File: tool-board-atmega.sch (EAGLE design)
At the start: 86 parts, among them IC3 ATMEGA2560-16AU, IC4 ATMEGA8U2-MU, Q1 16MHz, X1 22-23-2041, X2 MICROUSB_VERTICAL, X3 22-23-2041, X4 22-23-2041, Y2 16MHz

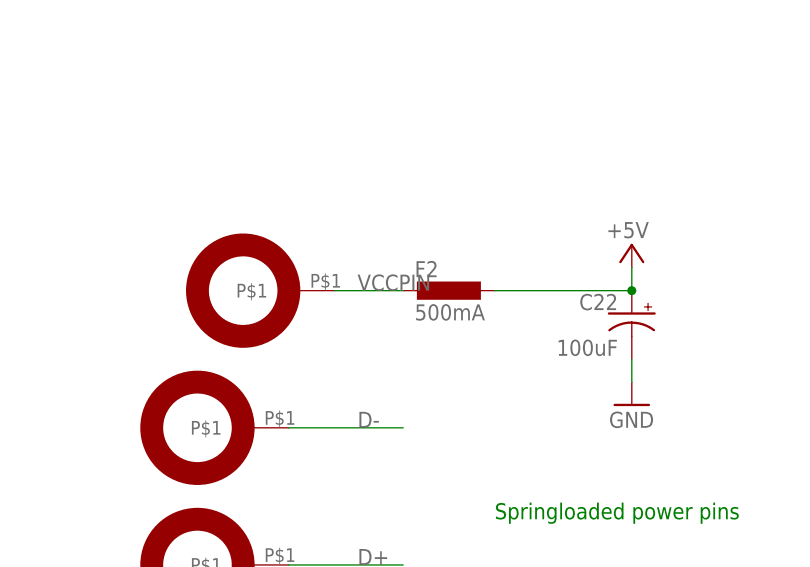
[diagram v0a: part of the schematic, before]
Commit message: significant routing done, need to beef up stepper related lines, add 24V stepper
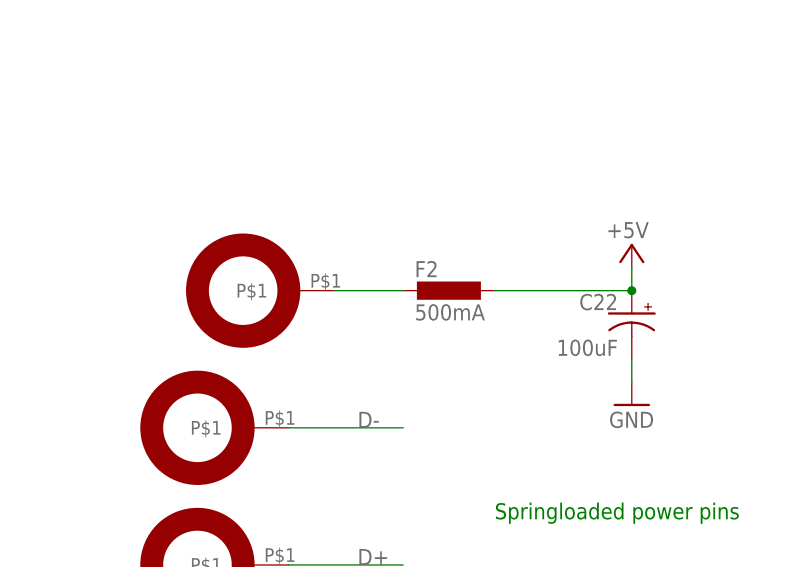
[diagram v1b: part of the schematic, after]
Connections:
- new net N$38: F2.2, U$9.P$1
- net VCCPIN: no longer F2.2, U$9.P$1
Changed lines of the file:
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@@
 <pinref part="X2" gate="G$1" pin="1"/>
-</segment>
-<segment>
-<pinref part="U$9" gate="G$1" pin="P$1"/>
-<wire x1="398.78" y1="-25.4" x2="406.4" y2="-25.4" width="0.1524" layer="91"/>
-<label x="401.32" y="-25.4" size="1.778" layer="95"/>
-<pinref part="F2" gate="G$1" pin="2"/>
 </segment>
 </net>
@@
 </segment>
 </net>
+<net name="N$38" class="0">
+<segment>
+<pinref part="U$9" gate="G$1" pin="P$1"/>
+<pinref part="F2" gate="G$1" pin="2"/>
+<wire x1="398.78" y1="-25.4" x2="406.4" y2="-25.4" width="0.1524" layer="91"/>
+</segment>
+</net>

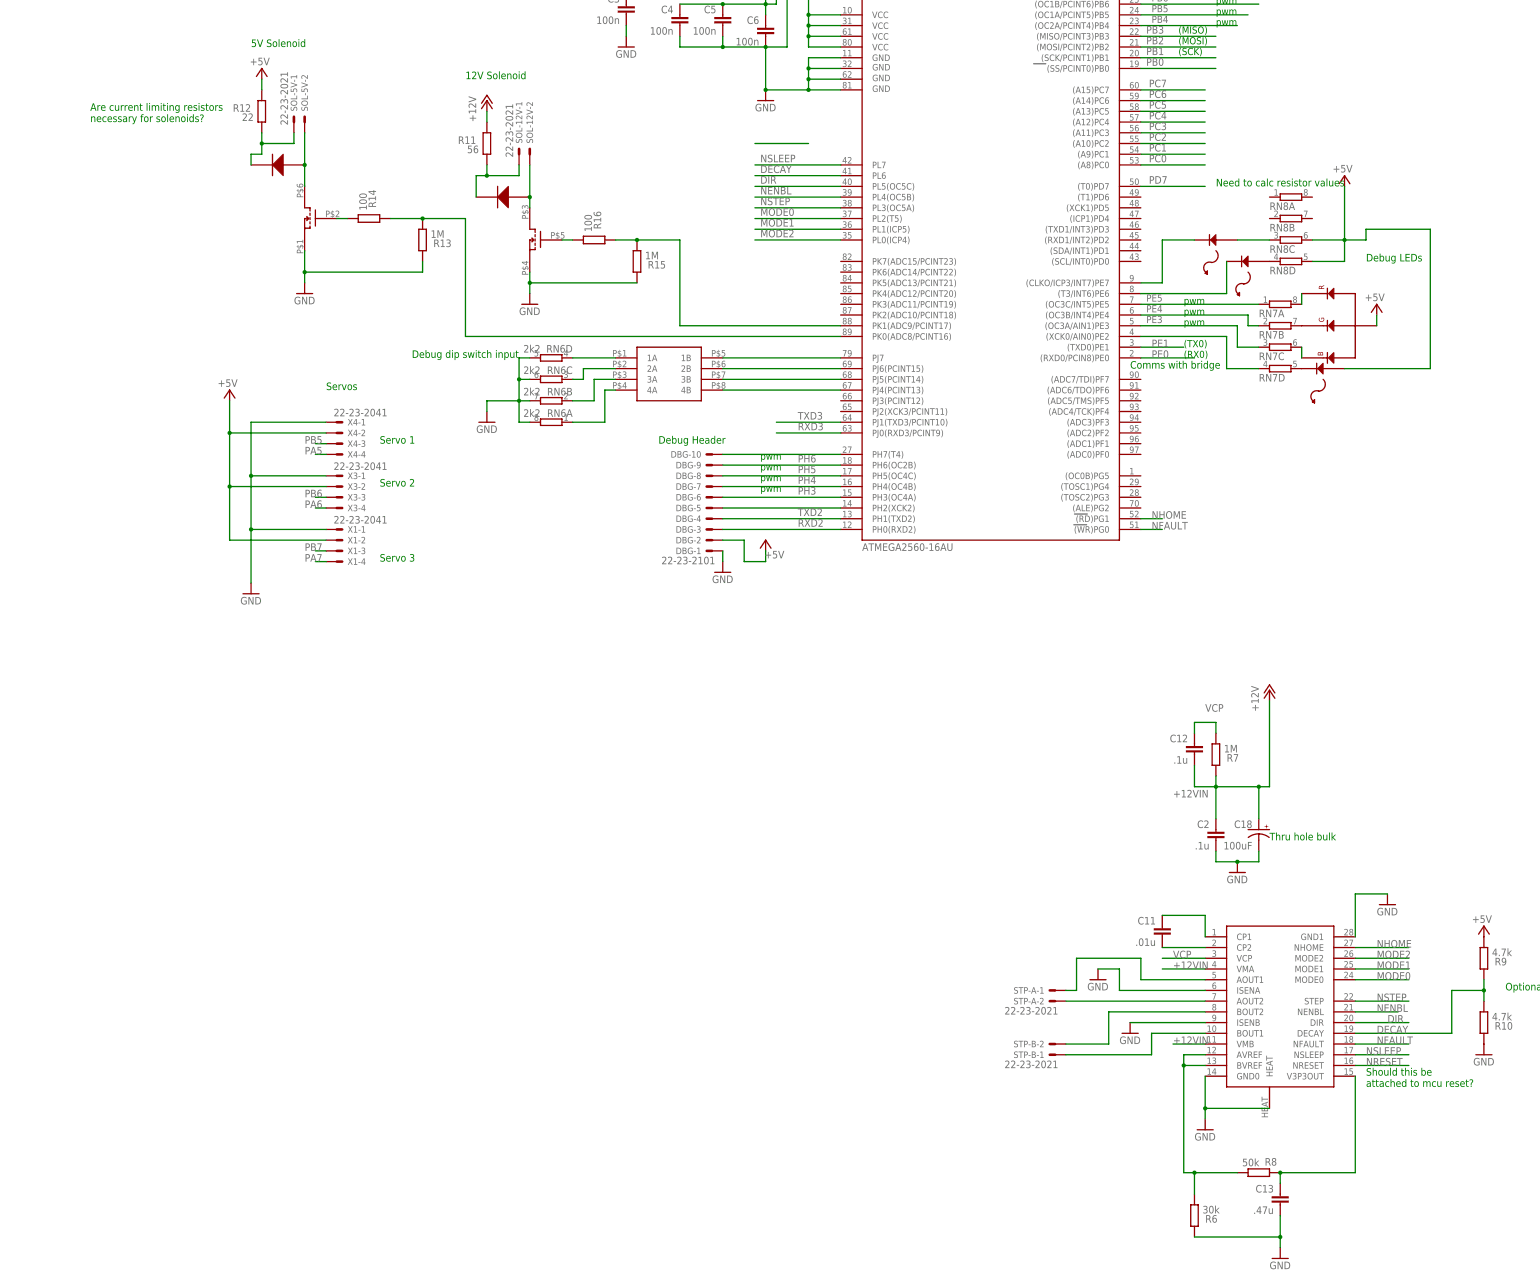
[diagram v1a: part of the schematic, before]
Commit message: Beefed up 12V stepper lines, still need to work on 24V stepper lines.  Need to switch connectors for higher current ones
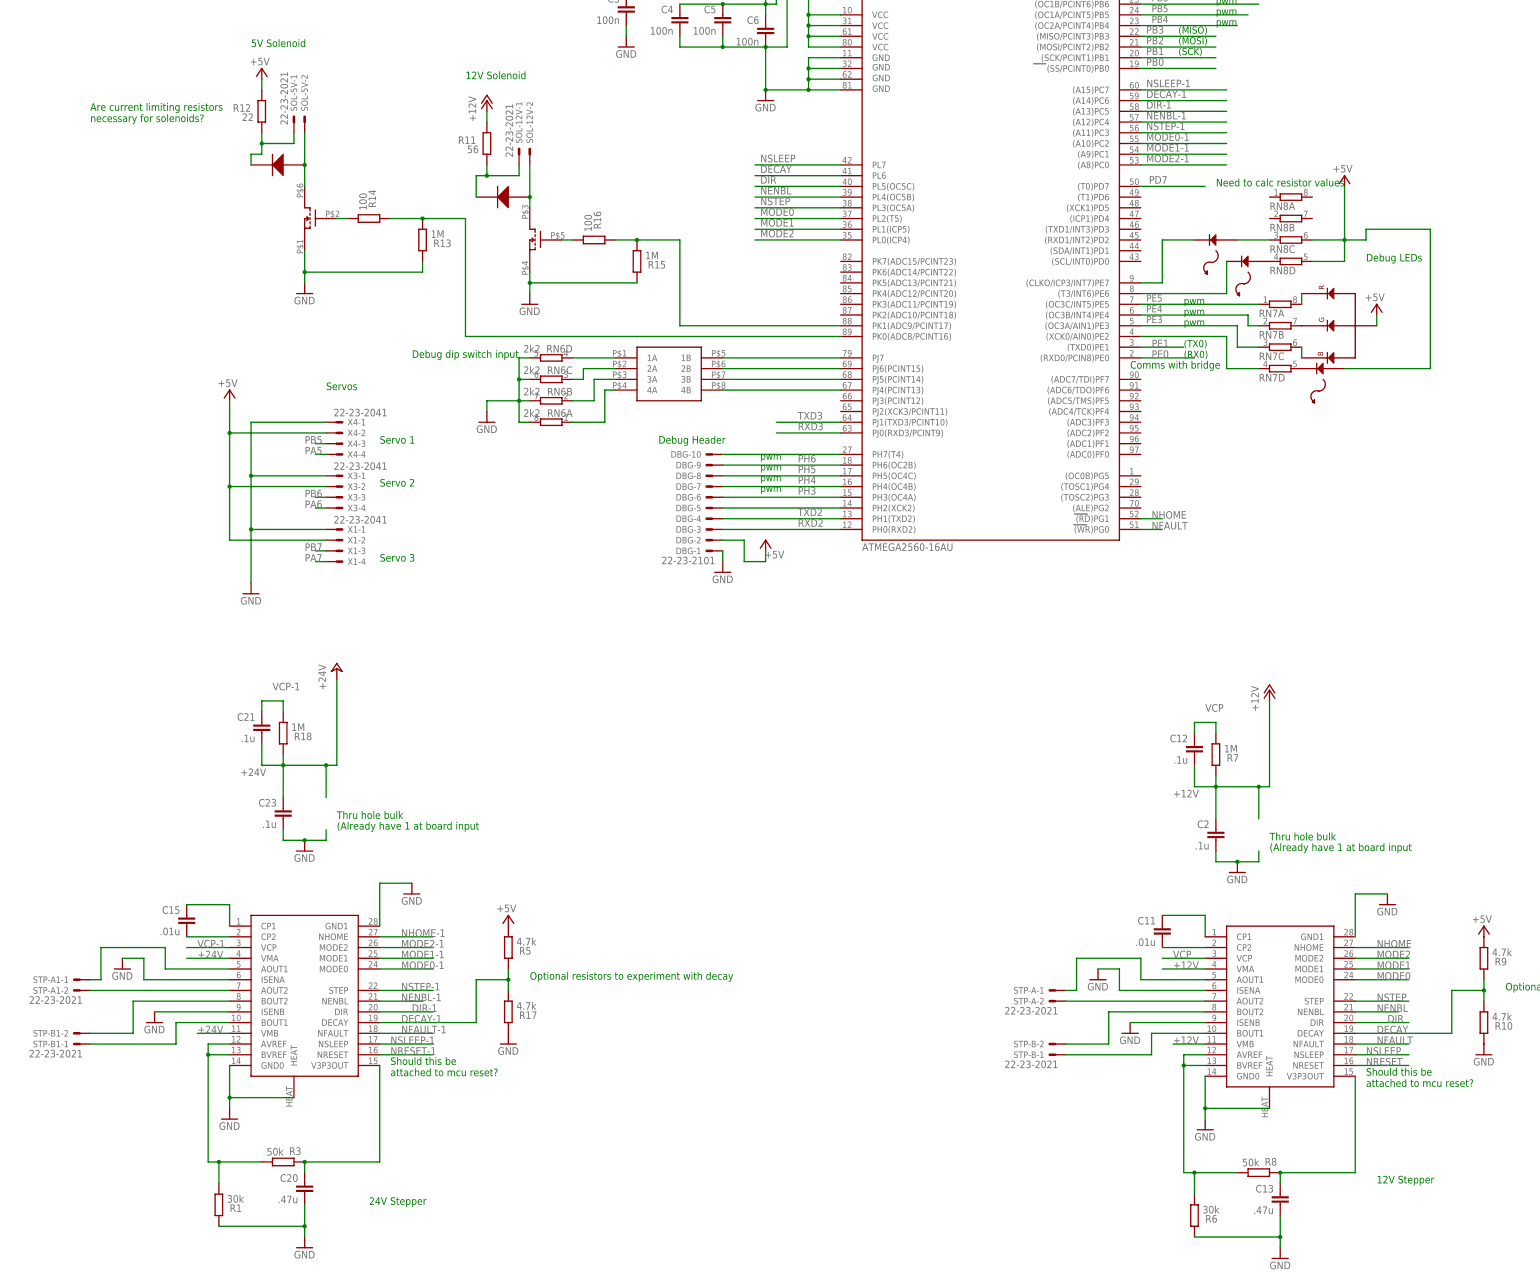
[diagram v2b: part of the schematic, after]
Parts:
- removed C18: 100uF, rcl:CPOL-USE3.5-8
- added C15: .01u, SmartPrj:C-EU0603-RND
- added C20: .47u, SmartPrj:C-EU0603-RND
- added C21, C23: .1u, SmartPrj:C-EU0603-RND
- added R1: 30k, SmartPrj:R-EU_R0603
- added R17, R5: 4.7k, SmartPrj:R-EU_R0603
- added R18: 1M, SmartPrj:R-EU_R0603
- added R3: 50k, SmartPrj:R-EU_R0603
- added STP-A1, STP-B1: 22-23-2021, con-molex:22-23-2021
- added U$7: DRV8825, ClinicalRobotics:DRV8825
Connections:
- removed net +12VIN: C12.2, C18.+, C2.1, R7.2, U$1.VMA, U$1.VMB
- removed net PC0: IC3.(A8)PC0
- removed net PC1: IC3.(A9)PC1
- removed net PC2: IC3.(A10)PC2
- removed net PC3: IC3.(A11)PC3
- removed net PC4: IC3.(A12)PC4
- removed net PC5: IC3.(A13)PC5
- removed net PC6: IC3.(A14)PC6
- removed net PC7: IC3.(A15)PC7
- new net DECAY-1: IC3.(A14)PC6, R17.1, R5.2, U$7.DECAY
- new net DIR-1: IC3.(A13)PC5, U$7.DIR
- new net MODE0-1: IC3.(A10)PC2, U$7.MODE0
- new net MODE1-1: IC3.(A9)PC1, U$7.MODE1
- new net MODE2-1: IC3.(A8)PC0, U$7.MODE2
- new net N$39: C15.1, U$7.CP1
- new net N$40: C15.2, U$7.CP2
- new net N$41: C20.1, R3.2, U$7.V3P3OUT
- new net N$42: R1.1, R3.1, U$7.AVREF, U$7.BVREF
- new net N$43: STP-A1-1.S, U$7.AOUT1
- new net N$44: STP-A1-2.S, U$7.AOUT2
- new net N$45: STP-B1-2.S, U$7.BOUT2
- new net N$46: STP-B1-1.S, U$7.BOUT1
- new net NENBL-1: IC3.(A12)PC4, U$7.NENBL
- new net NFAULT-1: U$7.NFAULT
- new net NHOME-1: U$7.NHOME
- new net NRESET-1: U$7.NRESET
- new net NSLEEP-1: IC3.(A15)PC7, U$7.NSLEEP
- new net NSTEP-1: IC3.(A11)PC3, U$7.STEP
- new net VCP-1: C21.1, R18.1, U$7.VCP
- net +12V: now also C12.2, C2.1, R7.2, U$1.VMA, U$1.VMB
- net +24V: now also C21.2, C23.1, R18.2, U$7.VMA, U$7.VMB
- net +5V: now also R5.1
- net GND: now also C20.2, C23.2, R1.2, R17.2, U$7.GND0, U$7.GND1, U$7.HEAT, U$7.ISENA, U$7.ISENB; no longer C18.-
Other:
- note added: "(Already have 1 at board input"
- note added: "12V Stepper"
- note added: "24V Stepper"

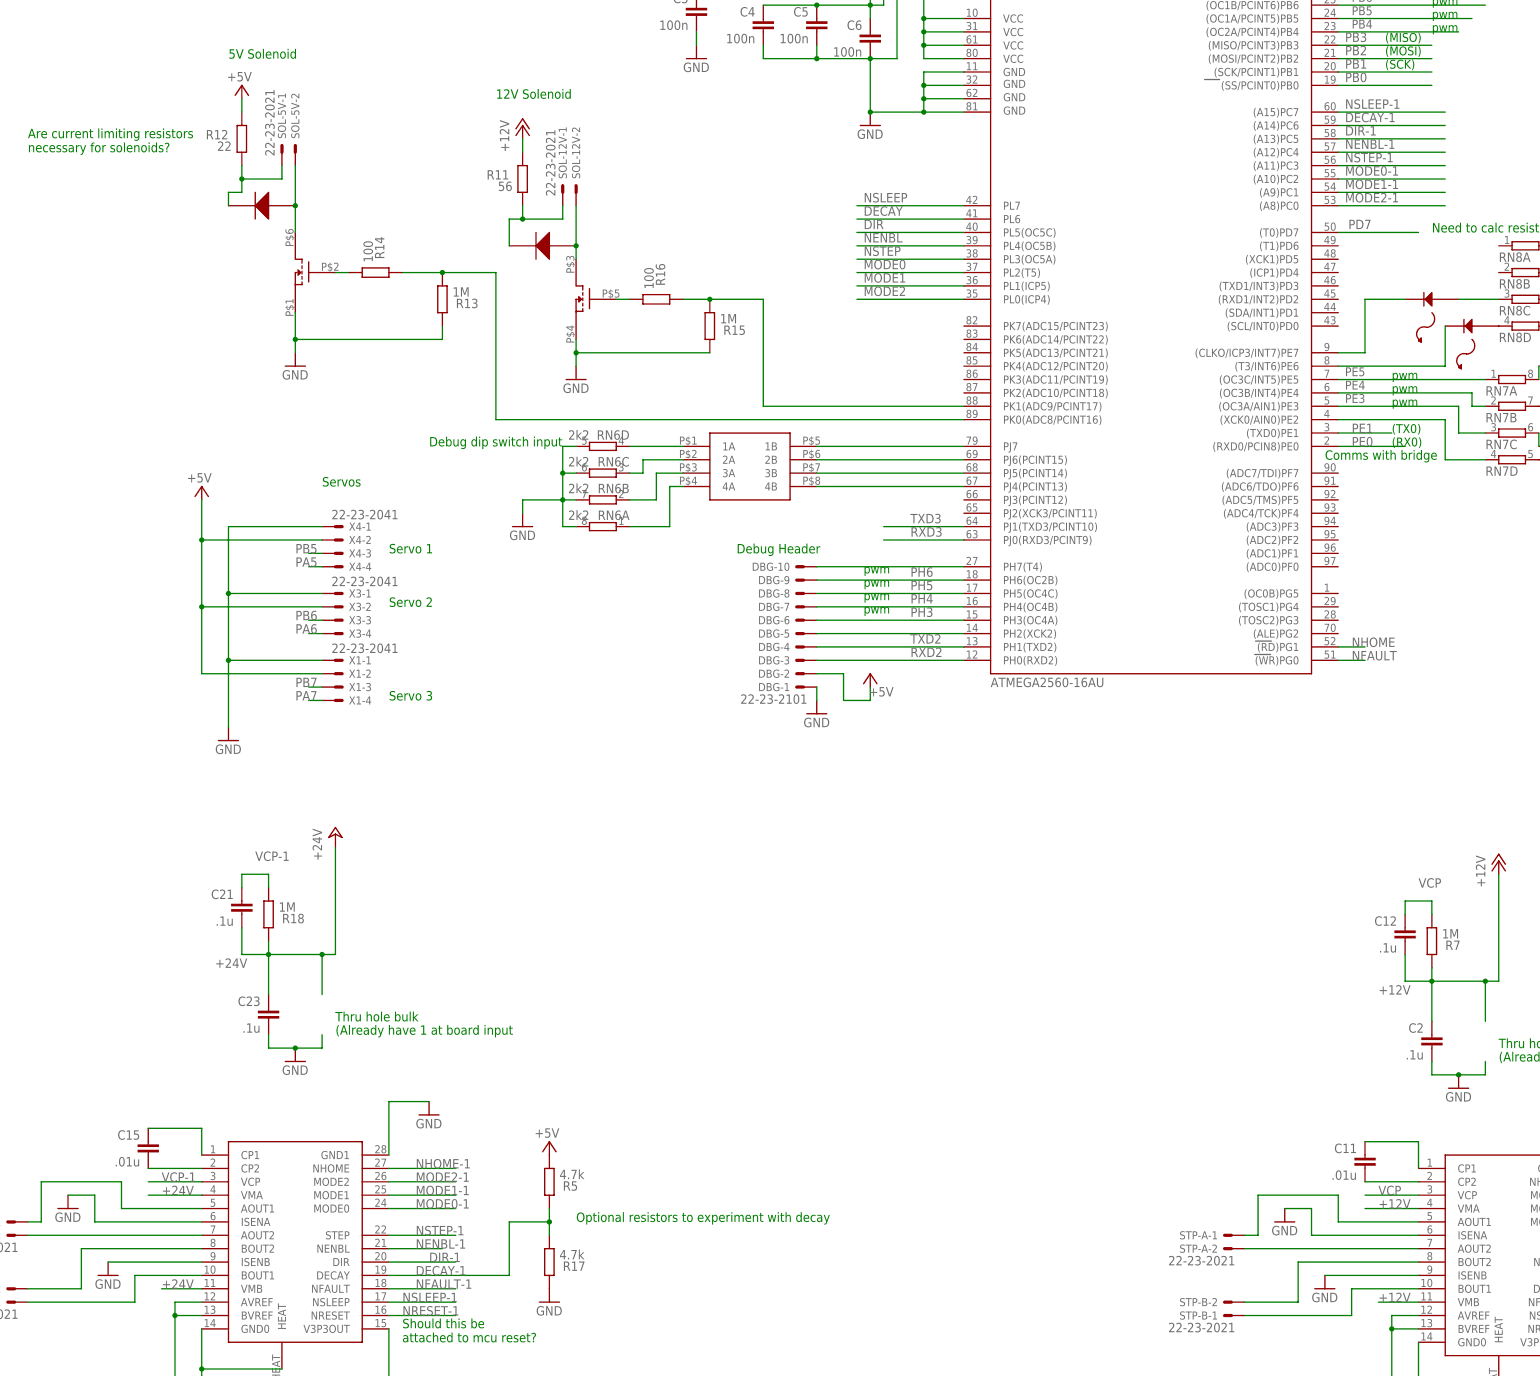
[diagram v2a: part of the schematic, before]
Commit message: Fixed stepper motor drivers for cleaner routing, moved them closer to power pogos
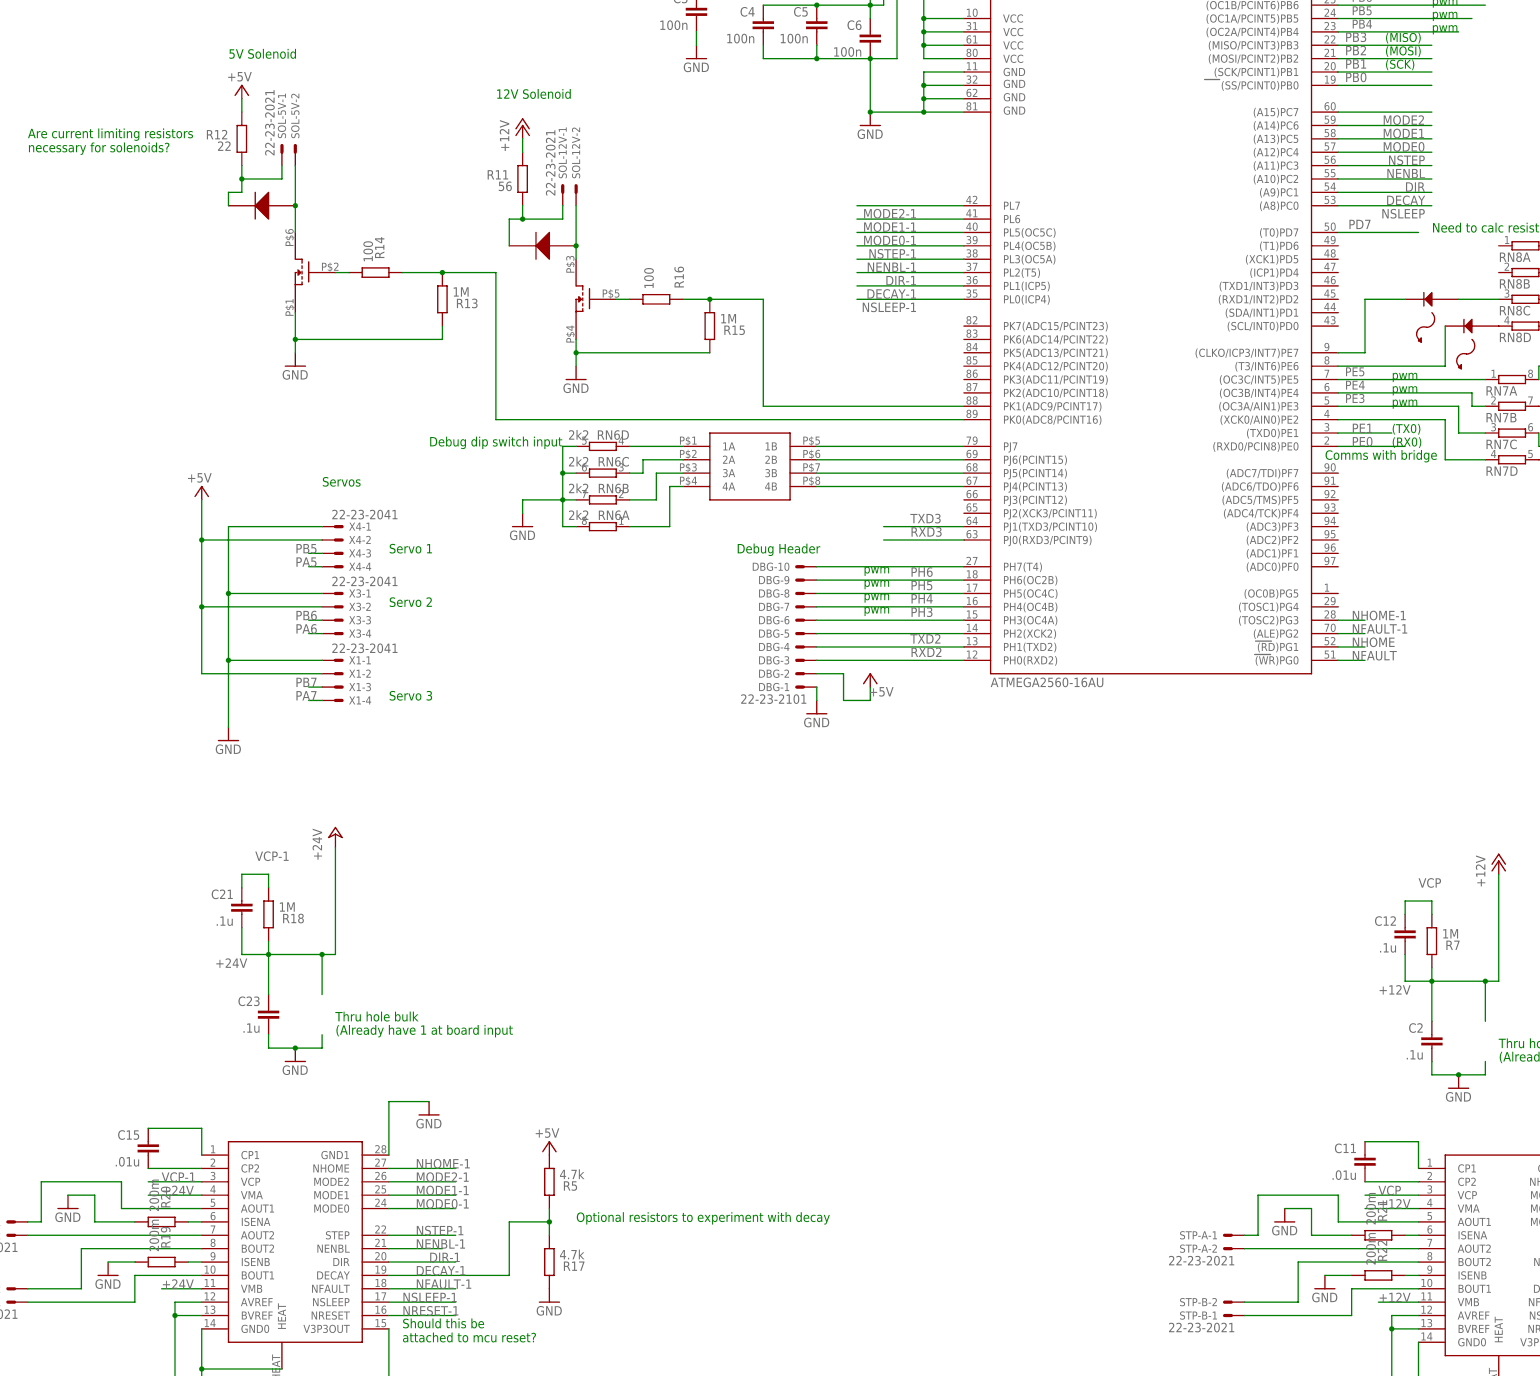
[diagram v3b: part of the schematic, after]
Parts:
- added R19, R20, R21, R22: 200m, SmartPrj:R-EU_R0603
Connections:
- new net N$37: R19.2, U$7.ISENB
- new net N$47: R20.2, U$7.ISENA
- new net N$48: R21.2, U$1.ISENA
- new net N$49: R22.2, U$1.ISENB
- net DECAY: now also IC3.(A9)PC1; no longer IC3.PL6
- net DECAY-1: now also IC3.PL1(ICP5); no longer IC3.(A14)PC6
- net DIR: now also IC3.(A10)PC2; no longer IC3.PL5(OC5C)
- net DIR-1: now also IC3.PL2(T5); no longer IC3.(A13)PC5
- net GND: now also R19.1, R20.1, R21.1, R22.1; no longer U$1.ISENA, U$1.ISENB, U$7.ISENA, U$7.ISENB
- net MODE0: now also IC3.(A13)PC5; no longer IC3.PL2(T5)
- net MODE0-1: now also IC3.PL5(OC5C); no longer IC3.(A10)PC2
- net MODE1: now also IC3.(A14)PC6; no longer IC3.PL1(ICP5)
- net MODE1-1: now also IC3.PL6; no longer IC3.(A9)PC1
- net MODE2: now also IC3.(A15)PC7; no longer IC3.PL0(ICP4)
- net MODE2-1: now also IC3.PL7; no longer IC3.(A8)PC0
- net NENBL: now also IC3.(A11)PC3; no longer IC3.PL4(OC5B)
- net NENBL-1: now also IC3.PL3(OC5A); no longer IC3.(A12)PC4
- net NFAULT-1: now also IC3.(ALE)PG2
- net NHOME-1: now also IC3.(TOSC2)PG3
- net NSLEEP: now also IC3.(A8)PC0; no longer IC3.PL7
- net NSLEEP-1: now also IC3.PL0(ICP4); no longer IC3.(A15)PC7
- net NSTEP: now also IC3.(A12)PC4; no longer IC3.PL3(OC5A)
- net NSTEP-1: now also IC3.PL4(OC5B); no longer IC3.(A11)PC3
